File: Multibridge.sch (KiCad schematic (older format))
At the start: 15 parts

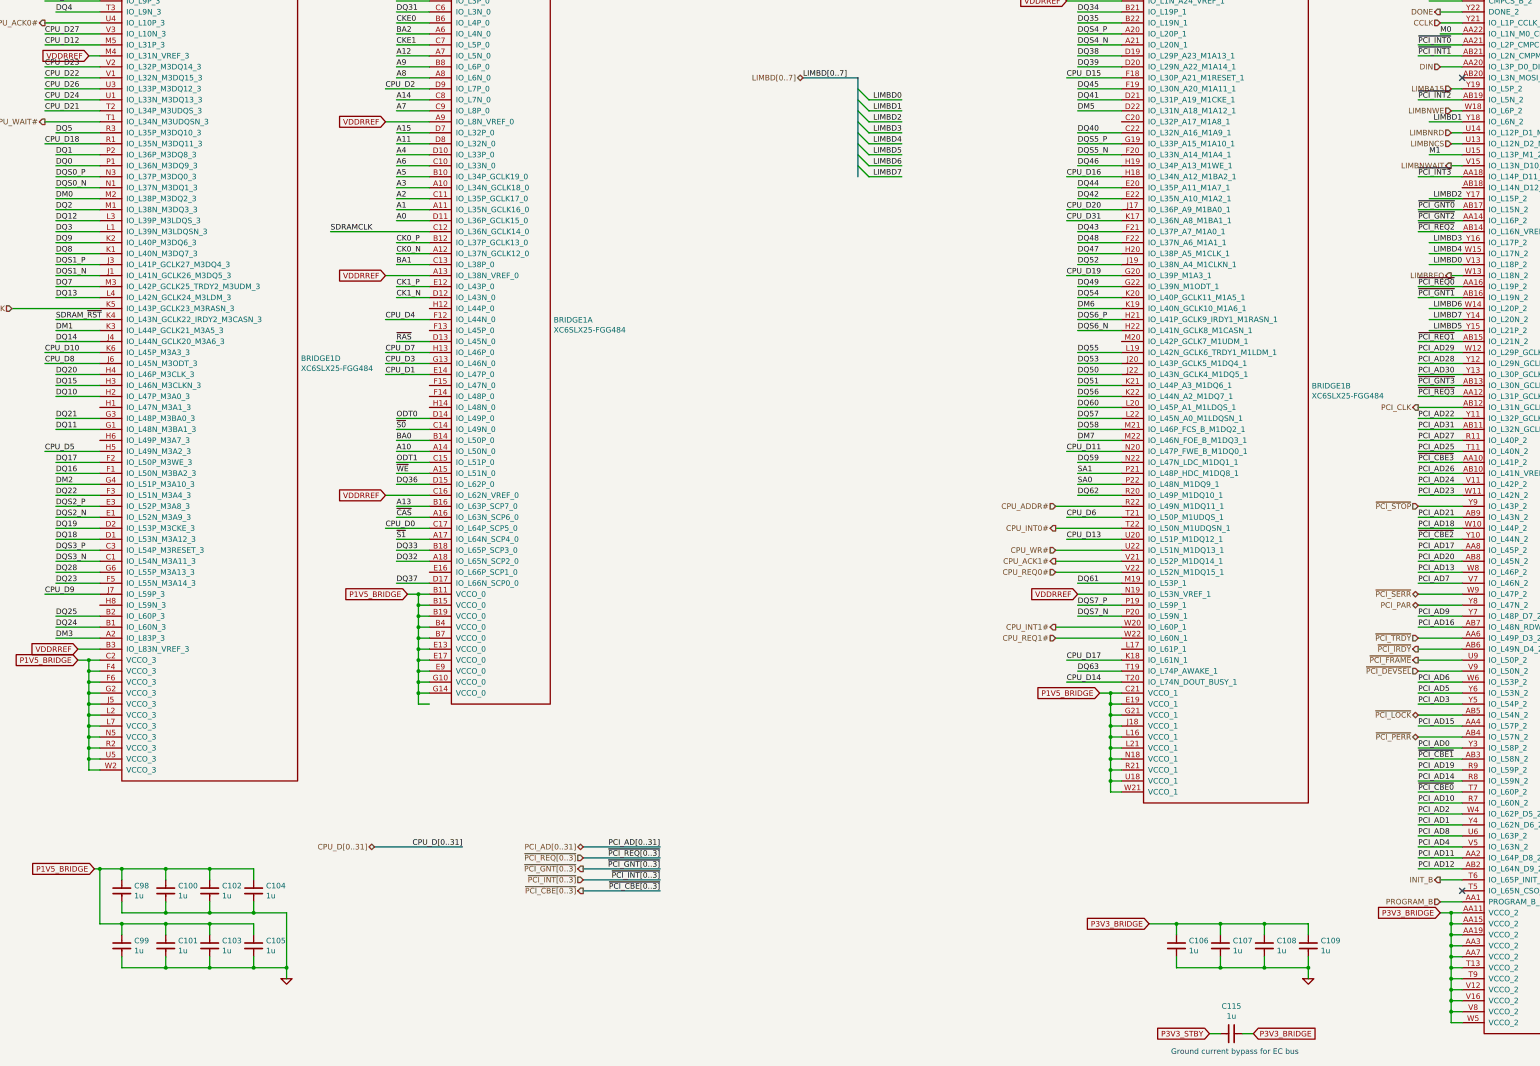
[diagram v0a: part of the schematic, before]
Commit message: Route clocks
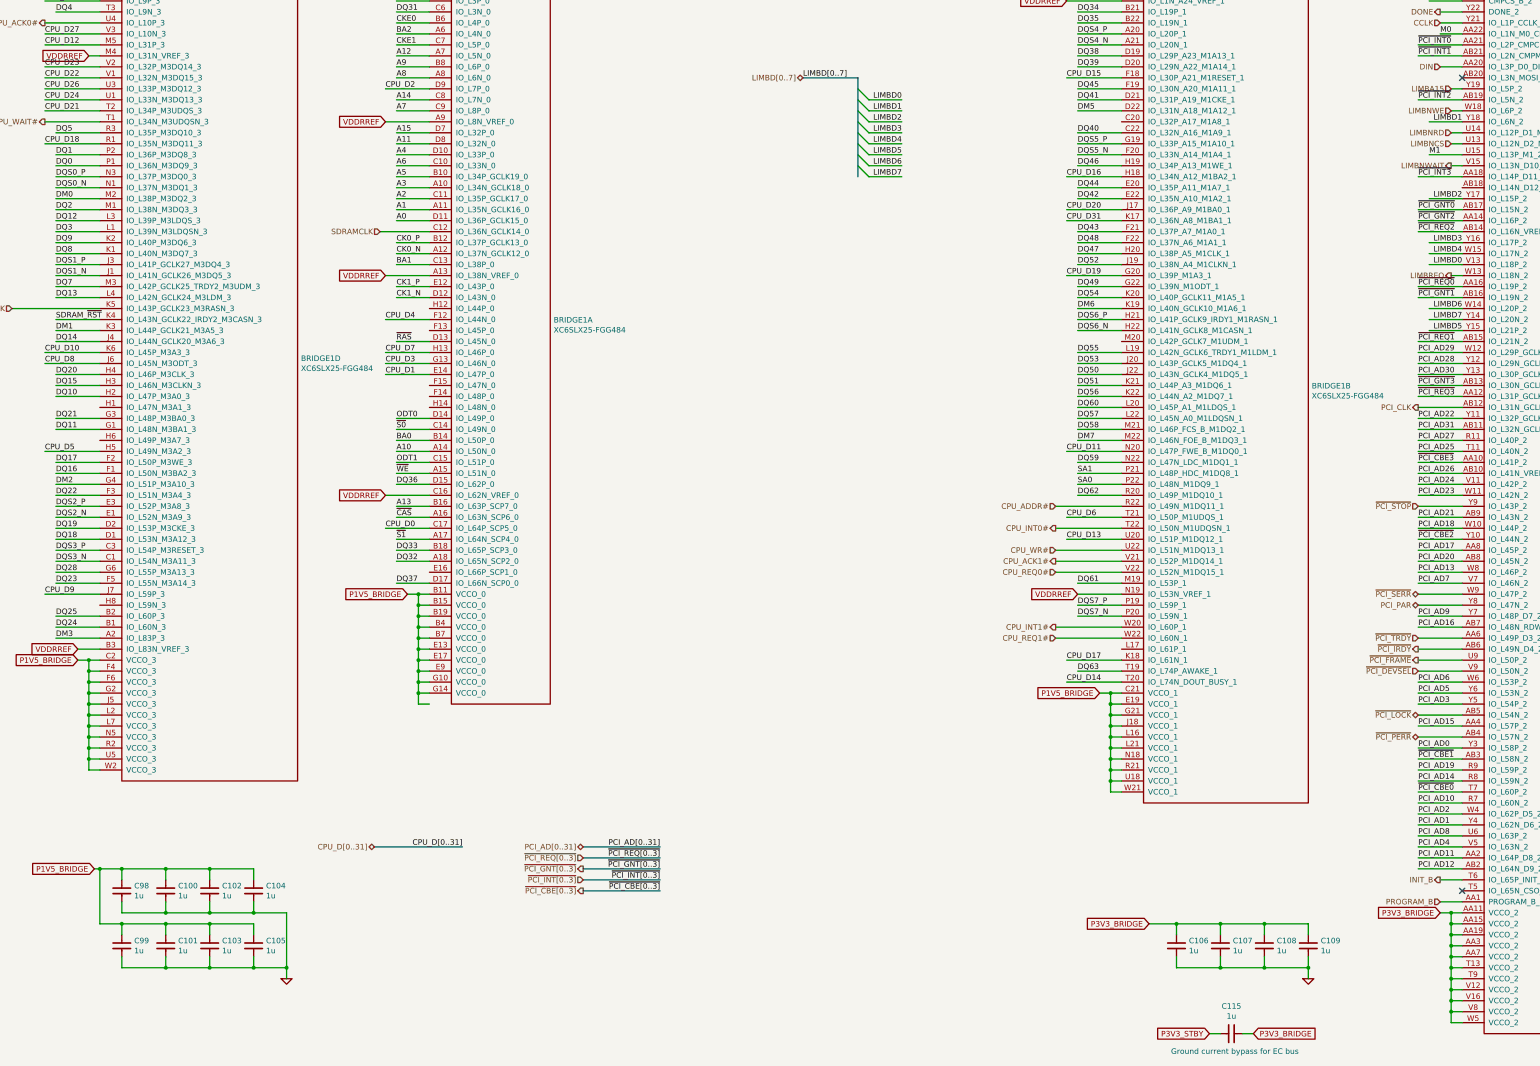
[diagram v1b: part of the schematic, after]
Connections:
- wire segments 468 -> 527
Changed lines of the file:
@@
 $Descr A2 23386 16535
 encoding utf-8
-Sheet 9 10
+Sheet 8 10
 Title ""
 Date ""
@@
 Text Label 14000 1700 0    50   ~ 0
 CMPCS
-Text Label 4000 3800 0    50   ~ 0
-SDRAMCLK
 Text HLabel 4400 9400 0    50   BiDi ~ 0
 CPU_D[0..31]
@@
 	19600 8000 19000 8000
 Wire Wire Line
-	4700 7100 4900 7100
+	4700 7100 4800 7100
+Wire Wire Line
+	4800 7100 4900 7100
 Wire Wire Line
 	4800 7200 4900 7200
@@
 Connection ~ 4800 8000
 Wire Wire Line
-	4800 7100 4800 8100
+	4800 7100 4800 7200
+Wire Wire Line
+	4800 7200 4800 7300
+Wire Wire Line
+	4800 7300 4800 7400
+Wire Wire Line
+	4800 7400 4800 7500
+Wire Wire Line
+	4800 7500 4800 7600
+Wire Wire Line
+	4800 7600 4800 7700
+Wire Wire Line
+	4800 7700 4800 7800
+Wire Wire Line
+	4800 7800 4800 7900
+Wire Wire Line
+	4800 7900 4800 8000
+Wire Wire Line
+	4800 8000 4800 8100
 Wire Wire Line
 	1700 7600 1900 7600
@@
 	4500 6200 4900 6200
 Wire Wire Line
-	11000 8000 11200 8000
+	11000 8000 11100 8000
+Wire Wire Line
+	11100 8000 11200 8000
 Wire Wire Line
 	11100 8100 11200 8100
@@
 Connection ~ 11100 8800
 Wire Wire Line
-	11100 8000 11100 8900
+	11100 8000 11100 8100
+Wire Wire Line
+	11100 8100 11100 8200
+Wire Wire Line
+	11100 8200 11100 8300
+Wire Wire Line
+	11100 8300 11100 8400
+Wire Wire Line
+	11100 8400 11100 8500
+Wire Wire Line
+	11100 8500 11100 8600
+Wire Wire Line
+	11100 8600 11100 8700
+Wire Wire Line
+	11100 8700 11100 8800
+Wire Wire Line
+	11100 8800 11100 8900
 Connection ~ 11100 8000
 Wire Wire Line
@@
 Connection ~ 14200 10900
 Wire Wire Line
-	14200 10000 14200 11000
-Wire Wire Line
-	1700 7700 1900 7700
+	14200 10000 14200 10100
+Wire Wire Line
+	14200 10100 14200 10200
+Wire Wire Line
+	14200 10200 14200 10300
+Wire Wire Line
+	14200 10300 14200 10400
+Wire Wire Line
+	14200 10400 14200 10500
+Wire Wire Line
+	14200 10500 14200 10600
+Wire Wire Line
+	14200 10600 14200 10700
+Wire Wire Line
+	14200 10700 14200 10800
+Wire Wire Line
+	14200 10800 14200 10900
+Wire Wire Line
+	14200 10900 14200 11000
+Wire Wire Line
+	1700 7700 1800 7700
+Wire Wire Line
+	1800 7700 1900 7700
 Wire Wire Line
 	1800 7800 1900 7800
@@
 Connection ~ 1800 8600
 Wire Wire Line
-	1800 7700 1800 8700
+	1800 7700 1800 7800
+Wire Wire Line
+	1800 7800 1800 7900
+Wire Wire Line
+	1800 7900 1800 8000
+Wire Wire Line
+	1800 8000 1800 8100
+Wire Wire Line
+	1800 8100 1800 8200
+Wire Wire Line
+	1800 8200 1800 8300
+Wire Wire Line
+	1800 8300 1800 8400
+Wire Wire Line
+	1800 8400 1800 8500
+Wire Wire Line
+	1800 8500 1800 8600
+Wire Wire Line
+	1800 8600 1800 8700
 Wire Wire Line
 	8900 2600 9200 2600
@@
 	8900 3300 9200 3300
 Wire Bus Line
-	8800 2400 8800 3300
+	8800 2400 8800 2500
+Wire Bus Line
+	8800 2500 8800 2600
+Wire Bus Line
+	8800 2600 8800 2700
+Wire Bus Line
+	8800 2700 8800 2800
+Wire Bus Line
+	8800 2800 8800 2900
+Wire Bus Line
+	8800 2900 8800 3000
+Wire Bus Line
+	8800 3000 8800 3100
+Wire Bus Line
+	8800 3100 8800 3200
+Wire Bus Line
+	8800 3200 8800 3300
 Wire Bus Line
 	8800 2400 8300 2400
@@
 	14000 1700 14300 1700
 Wire Wire Line
-	14100 10000 14300 10000
+	14100 10000 14200 10000
+Wire Wire Line
+	14200 10000 14300 10000
 Wire Wire Line
 	14200 10100 14300 10100
@@
 	13900 7300 14300 7300
 Wire Wire Line
-	4900 3800 4000 3800
+	4900 3800 4450 3800
 Wire Bus Line
 	4400 9400 5200 9400
@@
 P 3600 10600
 AR Path="/5763AB3B/5799D8FC" Ref="#PWR?"  Part="1"
-AR Path="/5763A638/5799D8FC" Ref="#PWR162"  Part="1"
-F 0 "#PWR162" H 3600 10600 30  0001 C CNN
+AR Path="/5763A638/5799D8FC" Ref="#PWR160"  Part="1"
+F 0 "#PWR160" H 3600 10600 30  0001 C CNN
 F 1 "GND" H 3600 10530 30  0001 C CNN
 F 2 "" H 3600 10600 60  0000 C CNN
@@
 	3300 10100 3300 10200
 Wire Wire Line
-	1900 10100 3300 10100
+	1900 10100 2100 10100
+Wire Wire Line
+	2100 10100 2500 10100
+Wire Wire Line
+	2500 10100 2900 10100
+Wire Wire Line
+	2900 10100 3300 10100
 Wire Wire Line
 	1900 10100 1900 9600
 Wire Wire Line
-	1850 9600 3300 9600
+	1850 9600 1900 9600
+Wire Wire Line
+	1900 9600 2100 9600
+Wire Wire Line
+	2100 9600 2500 9600
+Wire Wire Line
+	2500 9600 2900 9600
+Wire Wire Line
+	2900 9600 3300 9600
 Wire Wire Line
 	3300 9600 3300 9700
@@
 	2100 9900 2100 10000
 Wire Wire Line
-	2100 10000 3600 10000
-Wire Wire Line
-	3600 10000 3600 10600
-Wire Wire Line
-	3600 10500 2100 10500
+	2100 10000 2500 10000
+Wire Wire Line
+	2500 10000 2900 10000
+Wire Wire Line
+	2900 10000 3300 10000
+Wire Wire Line
+	3300 10000 3600 10000
+Wire Wire Line
+	3600 10000 3600 10500
+Wire Wire Line
+	3600 10500 3600 10600
+Wire Wire Line
+	3600 10500 3300 10500
+Wire Wire Line
+	3300 10500 2900 10500
+Wire Wire Line
+	2900 10500 2500 10500
+Wire Wire Line
+	2500 10500 2100 10500
 Wire Wire Line
 	2100 10500 2100 10400
@@
 $EndComp
 Wire Wire Line
-	11450 10100 12900 10100
+	11450 10100 11700 10100
+Wire Wire Line
+	11700 10100 12100 10100
+Wire Wire Line
+	12100 10100 12500 10100
+Wire Wire Line
+	12500 10100 12900 10100
 Wire Wire Line
 	12900 10100 12900 10200
@@
 	11700 10400 11700 10500
 Wire Wire Line
-	12900 10400 12900 10600
+	12900 10400 12900 10500
+Wire Wire Line
+	12900 10500 12900 10600
 Connection ~ 12900 10500
 Wire Wire Line
@@
 P3V3_BRIDGE
 $Comp
-L GND #PWR163
+L GND #PWR161
 U 1 1 5799E8A3
 P 12900 10600
-F 0 "#PWR163" H 12900 10600 30  0001 C CNN
+F 0 "#PWR161" H 12900 10600 30  0001 C CNN
 F 1 "GND" H 12900 10530 30  0001 C CNN
 F 2 "" H 12900 10600 60  0000 C CNN
@@
 $EndComp
 Wire Wire Line
-	11700 10500 12900 10500
+	11700 10500 12100 10500
+Wire Wire Line
+	12100 10500 12500 10500
+Wire Wire Line
+	12500 10500 12900 10500
 $Comp
 L C-0402 C?
@@
 Text Notes 11650 11300 0    50   ~ 0
 Ground current bypass for EC bus
+Text HLabel 4450 3800 0    50   Input ~ 0
+SDRAMCLK
 $EndSCHEMATC

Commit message: Add SDRAM SPD to I2C
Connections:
- net labels added: SCL, SDA
- net labels removed: SYS_SCL, SYS_SDA
- wire segments 527 -> 468
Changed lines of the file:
@@
 Text Label 19500 7600 2    50   ~ 0
 SDRAM_~RST
-Text Label 19500 7700 2    50   ~ 0
-SYS_SDA
-Text Label 19500 7800 2    50   ~ 0
-SYS_SCL
 Text Label 19500 7900 2    50   ~ 0
 ODT0
@@
 	19600 8000 19000 8000
 Wire Wire Line
-	4700 7100 4800 7100
-Wire Wire Line
-	4800 7100 4900 7100
+	4700 7100 4900 7100
 Wire Wire Line
 	4800 7200 4900 7200
@@
 Connection ~ 4800 8000
 Wire Wire Line
-	4800 7100 4800 7200
-Wire Wire Line
-	4800 7200 4800 7300
-Wire Wire Line
-	4800 7300 4800 7400
-Wire Wire Line
-	4800 7400 4800 7500
-Wire Wire Line
-	4800 7500 4800 7600
-Wire Wire Line
-	4800 7600 4800 7700
-Wire Wire Line
-	4800 7700 4800 7800
-Wire Wire Line
-	4800 7800 4800 7900
-Wire Wire Line
-	4800 7900 4800 8000
-Wire Wire Line
-	4800 8000 4800 8100
+	4800 7100 4800 8100
 Wire Wire Line
 	1700 7600 1900 7600
@@
 	4500 6200 4900 6200
 Wire Wire Line
-	11000 8000 11100 8000
-Wire Wire Line
-	11100 8000 11200 8000
+	11000 8000 11200 8000
 Wire Wire Line
 	11100 8100 11200 8100
@@
 Connection ~ 11100 8800
 Wire Wire Line
-	11100 8000 11100 8100
-Wire Wire Line
-	11100 8100 11100 8200
-Wire Wire Line
-	11100 8200 11100 8300
-Wire Wire Line
-	11100 8300 11100 8400
-Wire Wire Line
-	11100 8400 11100 8500
-Wire Wire Line
-	11100 8500 11100 8600
-Wire Wire Line
-	11100 8600 11100 8700
-Wire Wire Line
-	11100 8700 11100 8800
-Wire Wire Line
-	11100 8800 11100 8900
+	11100 8000 11100 8900
 Connection ~ 11100 8000
 Wire Wire Line
@@
 Connection ~ 14200 10900
 Wire Wire Line
-	14200 10000 14200 10100
-Wire Wire Line
-	14200 10100 14200 10200
-Wire Wire Line
-	14200 10200 14200 10300
-Wire Wire Line
-	14200 10300 14200 10400
-Wire Wire Line
-	14200 10400 14200 10500
-Wire Wire Line
-	14200 10500 14200 10600
-Wire Wire Line
-	14200 10600 14200 10700
-Wire Wire Line
-	14200 10700 14200 10800
-Wire Wire Line
-	14200 10800 14200 10900
-Wire Wire Line
-	14200 10900 14200 11000
-Wire Wire Line
-	1700 7700 1800 7700
-Wire Wire Line
-	1800 7700 1900 7700
+	14200 10000 14200 11000
+Wire Wire Line
+	1700 7700 1900 7700
 Wire Wire Line
 	1800 7800 1900 7800
@@
 Connection ~ 1800 8600
 Wire Wire Line
-	1800 7700 1800 7800
-Wire Wire Line
-	1800 7800 1800 7900
-Wire Wire Line
-	1800 7900 1800 8000
-Wire Wire Line
-	1800 8000 1800 8100
-Wire Wire Line
-	1800 8100 1800 8200
-Wire Wire Line
-	1800 8200 1800 8300
-Wire Wire Line
-	1800 8300 1800 8400
-Wire Wire Line
-	1800 8400 1800 8500
-Wire Wire Line
-	1800 8500 1800 8600
-Wire Wire Line
-	1800 8600 1800 8700
+	1800 7700 1800 8700
 Wire Wire Line
 	8900 2600 9200 2600
@@
 	8900 3300 9200 3300
 Wire Bus Line
-	8800 2400 8800 2500
-Wire Bus Line
-	8800 2500 8800 2600
-Wire Bus Line
-	8800 2600 8800 2700
-Wire Bus Line
-	8800 2700 8800 2800
-Wire Bus Line
-	8800 2800 8800 2900
-Wire Bus Line
-	8800 2900 8800 3000
-Wire Bus Line
-	8800 3000 8800 3100
-Wire Bus Line
-	8800 3100 8800 3200
-Wire Bus Line
-	8800 3200 8800 3300
+	8800 2400 8800 3300
 Wire Bus Line
 	8800 2400 8300 2400
@@
 	14000 1700 14300 1700
 Wire Wire Line
-	14100 10000 14200 10000
-Wire Wire Line
-	14200 10000 14300 10000
+	14100 10000 14300 10000
 Wire Wire Line
 	14200 10100 14300 10100
@@
 	3300 10100 3300 10200
 Wire Wire Line
-	1900 10100 2100 10100
-Wire Wire Line
-	2100 10100 2500 10100
-Wire Wire Line
-	2500 10100 2900 10100
-Wire Wire Line
-	2900 10100 3300 10100
+	1900 10100 3300 10100
 Wire Wire Line
 	1900 10100 1900 9600
 Wire Wire Line
-	1850 9600 1900 9600
-Wire Wire Line
-	1900 9600 2100 9600
-Wire Wire Line
-	2100 9600 2500 9600
-Wire Wire Line
-	2500 9600 2900 9600
-Wire Wire Line
-	2900 9600 3300 9600
+	1850 9600 3300 9600
 Wire Wire Line
 	3300 9600 3300 9700
@@
 	2100 9900 2100 10000
 Wire Wire Line
-	2100 10000 2500 10000
-Wire Wire Line
-	2500 10000 2900 10000
-Wire Wire Line
-	2900 10000 3300 10000
-Wire Wire Line
-	3300 10000 3600 10000
-Wire Wire Line
-	3600 10000 3600 10500
-Wire Wire Line
-	3600 10500 3600 10600
-Wire Wire Line
-	3600 10500 3300 10500
-Wire Wire Line
-	3300 10500 2900 10500
-Wire Wire Line
-	2900 10500 2500 10500
-Wire Wire Line
-	2500 10500 2100 10500
+	2100 10000 3600 10000
+Wire Wire Line
+	3600 10000 3600 10600
+Wire Wire Line
+	2100 10500 3600 10500
 Wire Wire Line
 	2100 10500 2100 10400
@@
 $EndComp
 Wire Wire Line
-	11450 10100 11700 10100
-Wire Wire Line
-	11700 10100 12100 10100
-Wire Wire Line
-	12100 10100 12500 10100
-Wire Wire Line
-	12500 10100 12900 10100
+	11450 10100 12900 10100
 Wire Wire Line
 	12900 10100 12900 10200
@@
 	11700 10400 11700 10500
 Wire Wire Line
-	12900 10400 12900 10500
-Wire Wire Line
-	12900 10500 12900 10600
+	12900 10400 12900 10600
 Connection ~ 12900 10500
 Wire Wire Line
-	12500 10400 12500 10500
+	12500 10500 12500 10400
 Connection ~ 12500 10500
 Wire Wire Line
@@
 $EndComp
 Wire Wire Line
-	11700 10500 12100 10500
-Wire Wire Line
-	12100 10500 12500 10500
-Wire Wire Line
-	12500 10500 12900 10500
+	11700 10500 12900 10500
 $Comp
 L C-0402 C?
@@
 Text HLabel 4450 3800 0    50   Input ~ 0
 SDRAMCLK
+Text HLabel 19600 7700 2    50   BiDi ~ 0
+SDA
+Text HLabel 19600 7800 2    50   Input ~ 0
+SCL
 $EndSCHEMATC

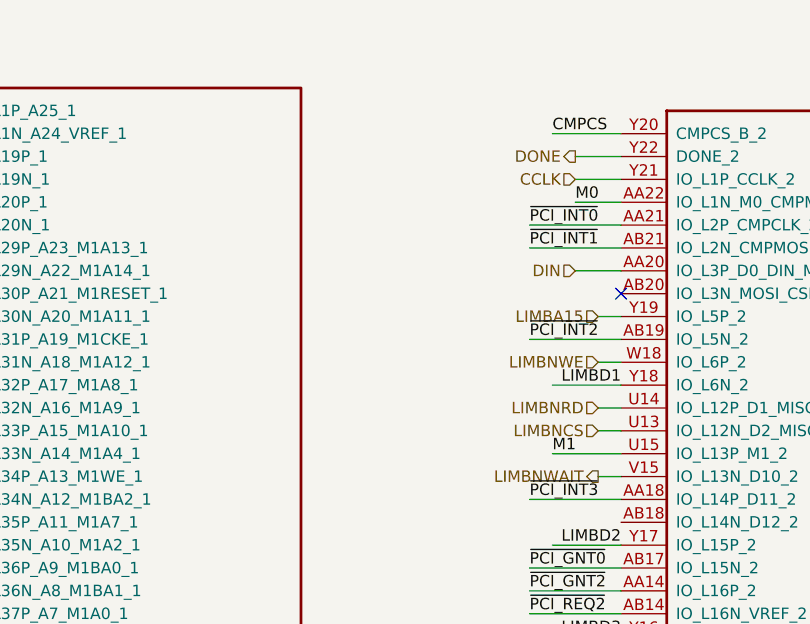
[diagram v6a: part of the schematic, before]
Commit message: Add configuration pullup resistors
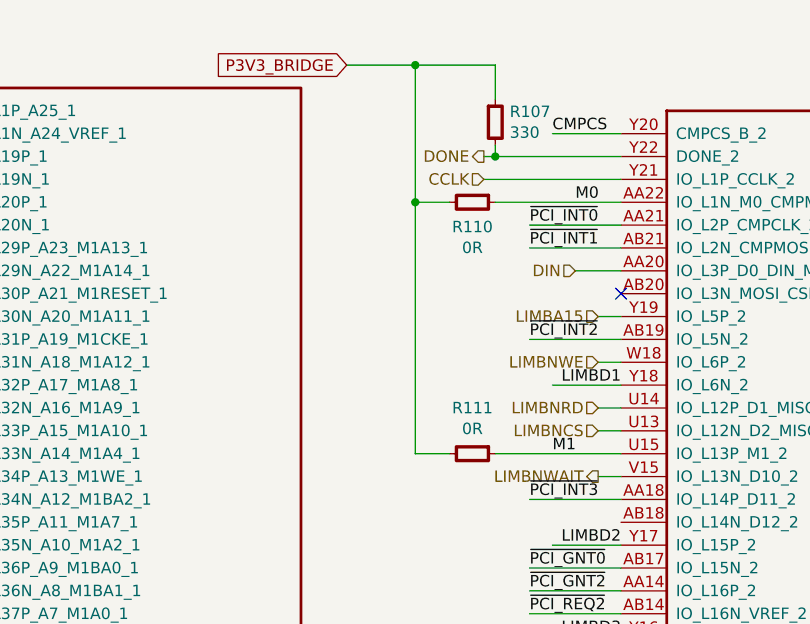
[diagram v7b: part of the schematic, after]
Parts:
- added R107: 330, IPC7351-Nominal:RESC1005X40, symbol R-0402
- added R110, R111: 0R, IPC7351-Nominal:RESC1005X40, symbol R-0402
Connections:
- wire segments 468 -> 474
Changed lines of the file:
@@
 Text HLabel 14100 9900 0    50   Input ~ 0
 PROGRAM_B
-Text HLabel 14100 1900 0    50   Input ~ 0
+Text HLabel 13700 1900 0    50   Input ~ 0
 CCLK
 Text HLabel 14100 2300 0    50   Input ~ 0
 DIN
-Text HLabel 14100 1800 0    50   Output ~ 0
+Text HLabel 13700 1800 0    50   Output ~ 0
 DONE
 Text HLabel 14100 9700 0    50   Output ~ 0
@@
 	14100 9900 14300 9900
 Wire Wire Line
-	14100 1900 14300 1900
+	13700 1900 14300 1900
 Wire Wire Line
 	14100 2300 14300 2300
 Wire Wire Line
-	14100 1800 14300 1800
+	13700 1800 14300 1800
 Wire Wire Line
 	14100 9700 14300 9700
@@
 	14200 3200 14300 3200
 Wire Wire Line
-	14300 2000 14100 2000
-Wire Wire Line
-	14300 3100 14000 3100
+	13750 2000 14300 2000
+Wire Wire Line
+	13750 3100 14300 3100
 Wire Wire Line
 	14000 1700 14300 1700
@@
 Text HLabel 19600 7800 2    50   Input ~ 0
 SCL
+$Comp
+L R-0402 R?
+U 1 1 57A59E23
+P 13750 1650
+AR Path="/5765A5BA/57A59E23" Ref="R?"  Part="1"
+AR Path="/5765B2E6/57A59E23" Ref="R?"  Part="1"
+AR Path="/5763A638/57A59E23" Ref="R107"  Part="1"
+F 0 "R107" H 13813 1696 50  0000 L CNN
+F 1 "330" H 13813 1605 50  0000 L CNN
+F 2 "IPC7351-Nominal:RESC1005X40" H 13750 1650 50  0001 C CNN
+F 3 "" H 13750 1700 60  0000 C CNN
+F 4 "RES SMD 330 1% [0402]" H 14500 2200 60  0001 C CNN "BOM"
+	1    13750 1650
+	1    0    0    -1
+$EndComp
+Wire Wire Line
+	13750 1750 13750 1800
+Connection ~ 13750 1800
+Text GLabel 13100 1400 0    50   Input ~ 0
+P3V3_BRIDGE
+Wire Wire Line
+	13100 1400 13750 1400
+Wire Wire Line
+	13750 1400 13750 1550
+$Comp
+L R-0402 R110
+U 1 1 57A5BAAA
+P 13650 2000
+F 0 "R110" V 13758 2000 50  0000 C CNN
+F 1 "0R" V 13849 2000 50  0000 C CNN
+F 2 "IPC7351-Nominal:RESC1005X40" H 13650 2000 50  0001 C CNN
+F 3 "" H 13650 2050 60  0000 C CNN
+F 4 "RES SMD 0R [0402]" H 14400 2550 60  0001 C CNN "BOM"
+	1    13650 2000
+	0    1    1    0
+$EndComp
+$Comp
+L R-0402 R111
+U 1 1 57A5BEA9
+P 13650 3100
+F 0 "R111" V 13450 3100 50  0000 C CNN
+F 1 "0R" V 13541 3100 50  0000 C CNN
+F 2 "IPC7351-Nominal:RESC1005X40" H 13650 3100 50  0001 C CNN
+F 3 "" H 13650 3150 60  0000 C CNN
+F 4 "RES SMD 0R [0402]" H 14400 3650 60  0001 C CNN "BOM"
+	1    13650 3100
+	0    1    1    0
+$EndComp
+Wire Wire Line
+	13400 3100 13550 3100
+Wire Wire Line
+	13400 1400 13400 3100
+Wire Wire Line
+	13400 2000 13550 2000
+Connection ~ 13400 1400
+Connection ~ 13400 2000
 $EndSCHEMATC
